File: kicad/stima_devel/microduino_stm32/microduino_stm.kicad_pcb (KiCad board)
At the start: 2 copper layers, 27.9 x 25.4 mm, 19 parts, among them IC1 STM32F103CBT6, J1 Conn_01x01, J2 USB_B_Micro, J3 Conn_01x01, SW1 SW_Push, SW2 SW_Push, U1 Microduino, U2 LP2985-3.3, Y1 8M, Y2 32.768KHz cl 12.5pF

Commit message: change diode footprint and update pcb
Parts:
- removed D2: D, Diode_SMD:D_0805_2012Metric
- added D1: D, Diode_SMD:D_SOD-123, F.Cu at (156.2, 161.4)
- moved R10 0.28 mm to (155.7, 159.1)
- moved SW1 0.25 mm to (150.7, 160.3)
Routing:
- net GND: track 83.4 -> 101.6 mm
- net /24_USBDM: track 4.77 -> 8.38 mm
- net +5V: track 22.6 -> 24.1 mm
- net /D4: track 5.31 -> 6.18 mm
- net /D6: track 18.9 -> 19.7 mm
- net Net-(IC1-Pad44): track 24.3 -> 23.8 mm

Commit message: bug: connect R5 to Vcc
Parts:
- turned R5 to 0 degrees
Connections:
- IC1 pad 2: (no net) -> Net-(IC1-Pad2)
- IC1 pad 25: (no net) -> Net-(IC1-Pad25)
- IC1 pad 26: (no net) -> Net-(IC1-Pad26)
- IC1 pad 27: (no net) -> Net-(IC1-Pad27)
- IC1 pad 28: (no net) -> Net-(IC1-Pad28)
- IC1 pad 41: (no net) -> Net-(IC1-Pad41)
- IC1 pad 45: (no net) -> Net-(IC1-Pad45)
- IC1 pad 46: (no net) -> Net-(IC1-Pad46)
- R5 pad 1: /23_USBDP -> +3V3
- R5 pad 2: GND -> /23_USBDP
- U2 pad 4: (no net) -> Net-(U2-Pad4)
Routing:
- net GND: track 101.6 -> 98.8 mm
- net +3V3: track 54.9 -> 56.6 mm, vias 8 -> 9

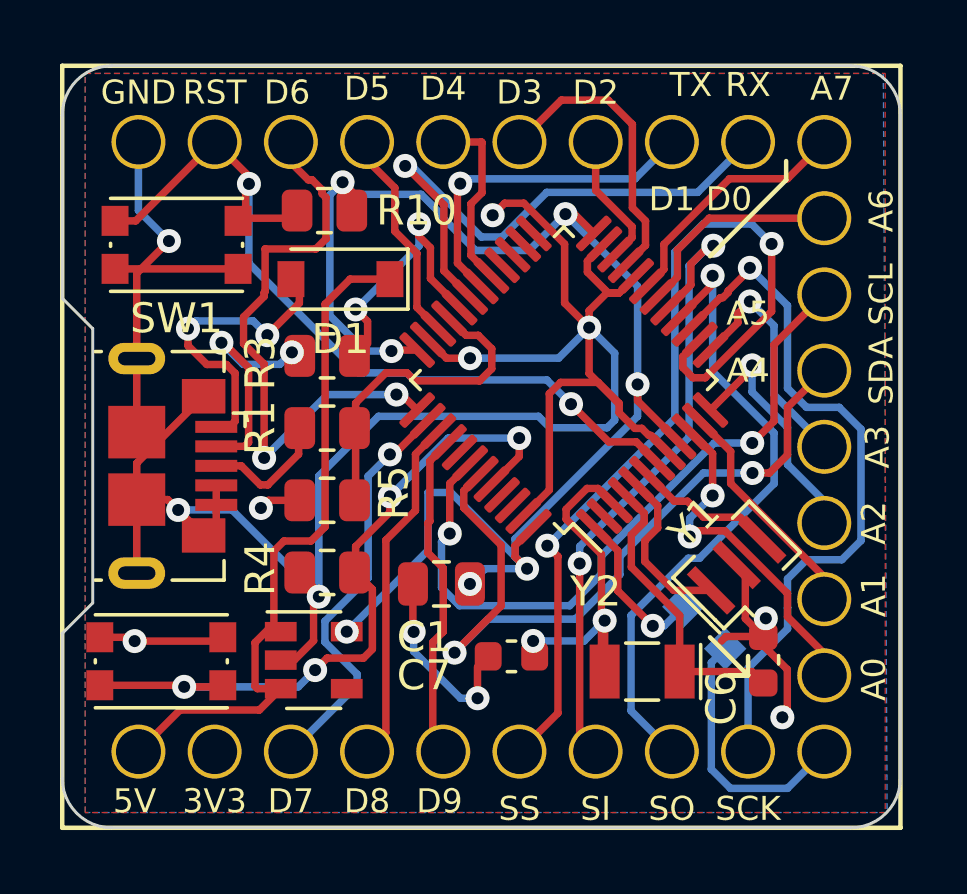
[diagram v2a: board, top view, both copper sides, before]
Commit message: Change D1 footprint
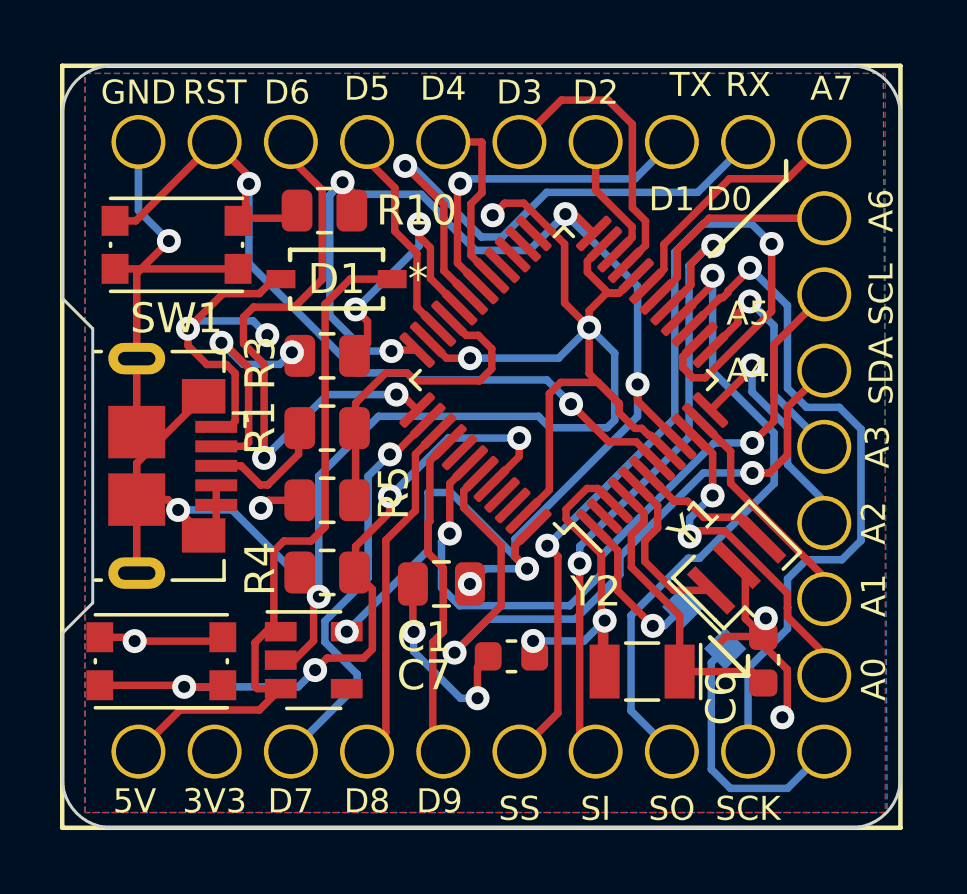
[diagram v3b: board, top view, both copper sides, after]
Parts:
- D1: footprint Diode_SMD:D_SOD-123 -> Diodo:STPS0530Z
- moved D1 0.13 mm to (156.1, 161.4)
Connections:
- IC1 pad 2: Net-(IC1-Pad2) -> (no net)
- IC1 pad 25: Net-(IC1-Pad25) -> (no net)
- IC1 pad 26: Net-(IC1-Pad26) -> (no net)
- IC1 pad 27: Net-(IC1-Pad27) -> (no net)
- IC1 pad 28: Net-(IC1-Pad28) -> (no net)
- IC1 pad 41: Net-(IC1-Pad41) -> (no net)
- IC1 pad 45: Net-(IC1-Pad45) -> (no net)
- IC1 pad 46: Net-(IC1-Pad46) -> (no net)
- U2 pad 4: Net-(U2-Pad4) -> (no net)
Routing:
- net Net-(D1-Pad2): track 10.00 -> 11.6 mm
